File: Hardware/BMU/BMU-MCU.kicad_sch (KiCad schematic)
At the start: 6 parts, among them IC1 STM32C092RCT6, J6 Conn_ARM_JTAG_SWD_10

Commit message: update power part
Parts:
- removed J6: Conn_ARM_JTAG_SWD_10, Connector_PinHeader_1.27mm:PinHeader_2x05_P1.27mm_Vertical, symbol Connector:Conn_ARM_JTAG_SWD_10
- added J12: Conn_ST_STDC14, Connector_PinHeader_1.27mm:PinHeader_2x07_P1.27mm_Vertical, symbol Connector:Conn_ST_STDC14
- renumbered R13 to R22
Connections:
- net +3V3: now also J12.3 (VCC)
- net GND: now also J12.11 (GNDDetect), J12.12 (~{RST}), J12.5 (GND)
- net at IC1.45 (PA13): now also J12.4 (JTMS/SWDIO)
- net at IC1.46 (PA14-BOOT0): now also J12.6 (JCLK/SWCLK)
- net SHUTDOWN: now reaches IC1.13 (PC0)
- net GPIO_SPARE1: now reaches IC1.14 (PC1)
- net GPIO_SPARE2: now reaches IC1.15 (PC2)
- net GPIO_SPARE3: now reaches IC1.16 (PC3)
- net at IC1.19 (PA2): now also J12.13 (VCP_RX)
- net at IC1.20 (PA3): now also J12.14 (VCP_TX)
- net SHUTDOWN_REQ renamed POWER_LED
- net STATUS_LED renamed FAULT_LED
- net UART_RX renamed UART1_RX
- net UART_TX renamed UART1_TX
- no-connect marks 49 -> 44
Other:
- note added: "| Function | MCU Pin | Notes | | ------------- | --------------- | ------------------------ | | SWDIO | PA13 | Debug/programming | | SWCLK | PA14 | Debug/programming, shared with BOOT0 pin | | NRST | PF2 | Hardware reset | | BQ UART TX | PB6 | MCU → BQ79600 | | BQ UART RX | PB7 | BQ79600 → MCU | | Shunt I2C SCL | PB8 | I2C1_SCL | | Shunt I2C SDA | PB9 | I2C1_SDA | | CAN RX | PD0 | FDCAN1_RX | | C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"
- note removed: "| Function | MCU Pin | Notes | | ------------- | --------------- | ---------------------------------------- | | SWDIO | PA13 | Debug/programming | | SWCLK | PA14 | Debug/programming, shared with BOOT0 pin | | NRST | PF2 | Hardware reset | | BQ UART TX | PB6 | MCU → BQ79600 | | BQ UART RX | PB7 | BQ79600 → MCU | | Shunt I2C SCL | PB8 | I2C1_SCL | | Shunt I2C SDA | PB9 | I2C1_SDA | | CAN RX | PD0 |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"

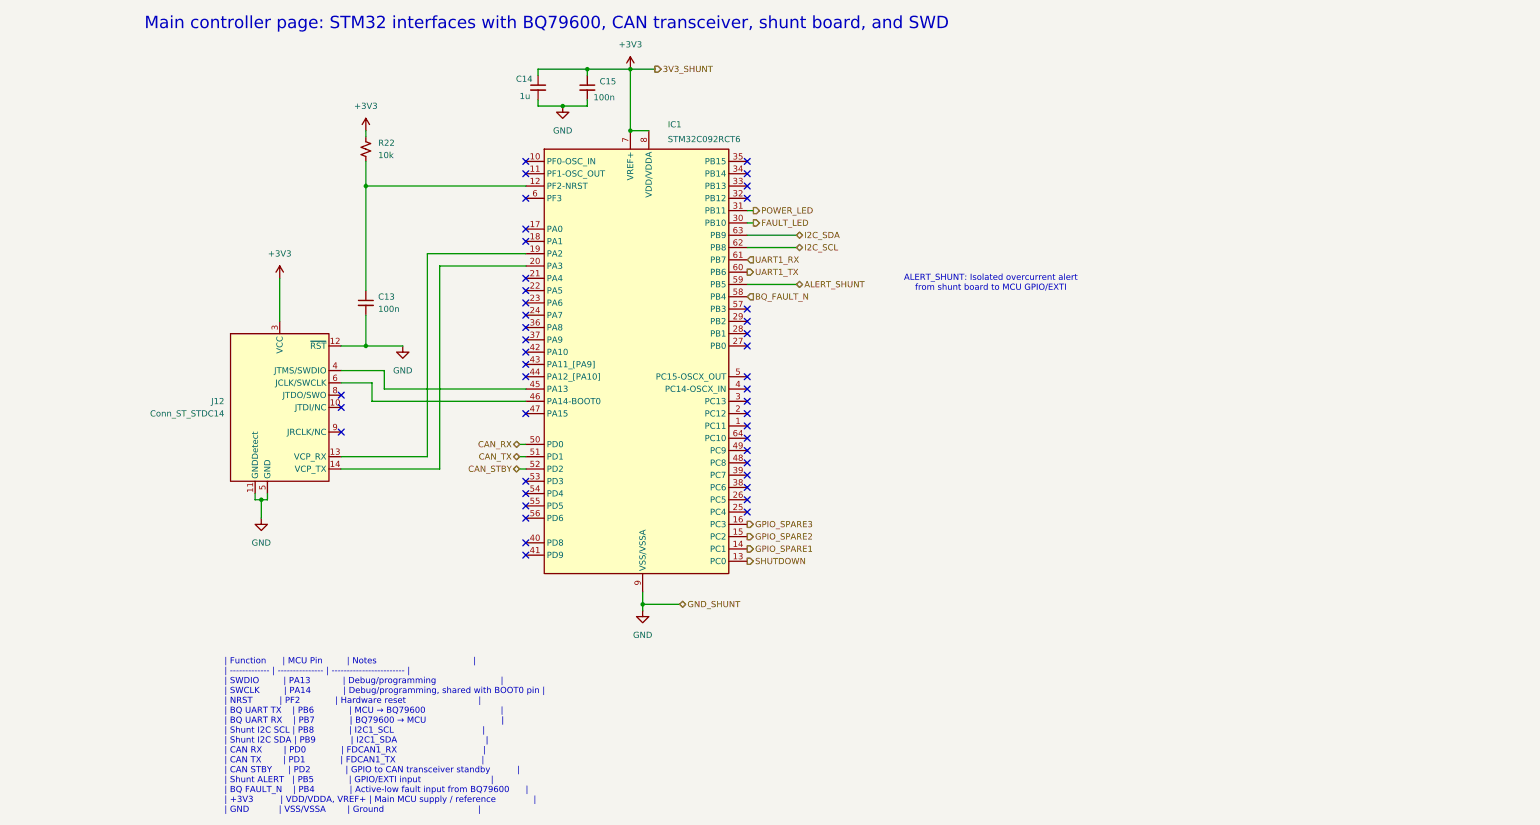
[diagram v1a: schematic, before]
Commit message: finish BMU, add test point + comment
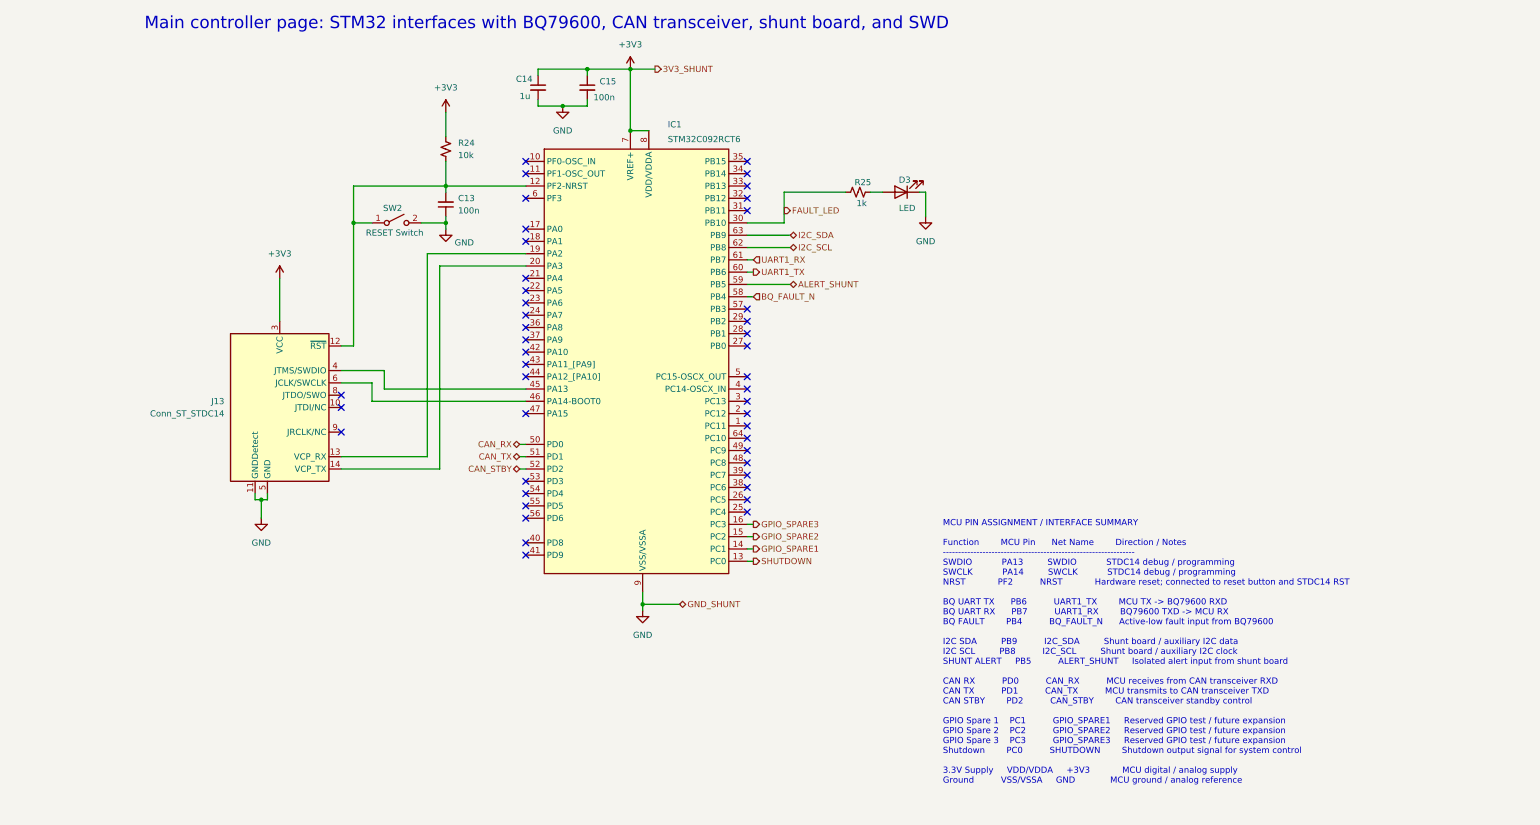
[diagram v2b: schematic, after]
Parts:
- added D3: LED, LED_SMD:LED_0805_2012Metric_Pad1.15x1.40mm_HandSolder, symbol Device:LED
- added R25: 1k, Resistor_SMD:R_0805_2012Metric, symbol Device:R_Small_US
- added SW2: RESET Switch, Button_Switch_SMD:SW_Push_1P1T_NO_CK_KMR2, symbol Switch:SW_SPST
- renumbered J12 to J13, R22 to R24
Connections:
- net FAULT_LED: now also R25.1
- net GND: now also C13.1, D3.1 (K), SW2.2 (B); no longer C13.2, J13.12 (~{RST})
- net at IC1.12 (PF2-NRST), R24.2: now also C13.2, J13.12 (~{RST}), SW2.1 (A); no longer C13.1
- net POWER_LED: no longer names the net of IC1.31 (PB11)
- new net: D3.2 (A), R25.2
- no-connect marks 44 -> 45
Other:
- note added: "MCU PIN ASSIGNMENT / INTERFACE SUMMARY Function MCU Pin Net Name Direction / Notes --------------------------------------------------------------- SWDIO PA13 SWDIO STDC14 debug / programming SWCLK PA14 SWCLK STDC14 debug / programming NRST PF2 NRST Hardware reset; connected to reset button and STDC14 RST BQ UART TX PB6 UART1_TX MCU TX -> BQ79600 RXD BQ UART RX PB7 UART1_RX BQ79600 TXD -> MCU RX B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"
- note removed: "ALERT_SHUNT: Isolated overcurrent alert from shunt board to MCU GPIO/EXTI"
- note removed: "| Function | MCU Pin | Notes | | ------------- | --------------- | ------------------------ | | SWDIO | PA13 | Debug/programming | | SWCLK | PA14 | Debug/programming, shared with BOOT0 pin | | NRST | PF2 | Hardware reset | | BQ UART TX | PB6 | MCU → BQ79600 | | BQ UART RX | PB7 | BQ79600 → MCU | | Shunt I2C SCL | PB8 | I2C1_SCL | | Shunt I2C SDA | PB9 | I2C1_SDA | | CAN RX | PD0 | FDCAN1_RX | | C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"
- moved on the sheet: C13, R24
